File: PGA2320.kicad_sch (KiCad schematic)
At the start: 20 parts, among them J1 XH2.54-3P, J2 XH2.54-3P, J3 2P-2.54, J4 3P-2.54, P1 SDO_TO_OTHER_PGA2311, P2 CONTROLLER, U1 PGA2320

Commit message: add libs
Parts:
- U1: symbol Amplifier_Audio:PGA2320 -> PGA2320_components:PGA2320
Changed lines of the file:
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@@
     )
   )
-  (symbol (lib_id "Amplifier_Audio:PGA2320") (at 140.97 39.37 0) (unit 1)
+  (symbol (lib_id "PGA2320_components:PGA2320") (at 140.97 39.37 0) (unit 1)
     (in_bom yes) (on_board yes) (dnp no)
     (property "Reference" "U1" (at 157.48 52.07 0)

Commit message: pcb layout
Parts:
- P1: footprint Connector_Pin:Pin_D0.7mm_L6.5mm_W1.8mm_FlatFork -> Connector_Pin:Pin_D0.9mm_L10.0mm_W2.4mm_FlatFork
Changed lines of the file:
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@@
       (effects (font (size 1.27 1.27)))
     )
-    (property "Footprint" "Connector_Pin:Pin_D0.7mm_L6.5mm_W1.8mm_FlatFork" (at 180.34 125.73 0)
+    (property "Footprint" "Connector_Pin:Pin_D0.9mm_L10.0mm_W2.4mm_FlatFork" (at 180.34 125.73 0)
       (effects (font (size 1.27 1.27)) hide)
     )

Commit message: layout
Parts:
- D1, D2, D3: footprint Audio_Module:Led_1206 -> LED_SMD:LED_0805_2012Metric_Pad1.15x1.40mm_HandSolder
- R1, R2, R3: footprint Audio_Module:r_1210 -> Resistor_SMD:R_0805_2012Metric_Pad1.20x1.40mm_HandSolder
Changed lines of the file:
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@@
       (effects (font (size 1.27 1.27)))
     )
-    (property "Footprint" "Audio_Module:Led_1206" (at 54.61 77.47 0)
+    (property "Footprint" "LED_SMD:LED_0805_2012Metric_Pad1.15x1.40mm_HandSolder" (at 54.61 77.47 0)
       (effects (font (size 1.27 1.27)) hide)
     )
@@
       (effects (font (size 1.27 1.27)))
     )
-    (property "Footprint" "Audio_Module:r_1210" (at 46.99 55.372 90)
+    (property "Footprint" "Resistor_SMD:R_0805_2012Metric_Pad1.20x1.40mm_HandSolder" (at 46.99 55.372 90)
       (effects (font (size 1.27 1.27)) hide)
     )
@@
       (effects (font (size 1.27 1.27)))
     )
-    (property "Footprint" "Audio_Module:Led_1206" (at 54.61 57.15 0)
+    (property "Footprint" "LED_SMD:LED_0805_2012Metric_Pad1.15x1.40mm_HandSolder" (at 54.61 57.15 0)
       (effects (font (size 1.27 1.27)) hide)
     )
@@
       (effects (font (size 1.27 1.27)))
     )
-    (property "Footprint" "Audio_Module:r_1210" (at 46.99 67.818 90)
+    (property "Footprint" "Resistor_SMD:R_0805_2012Metric_Pad1.20x1.40mm_HandSolder" (at 46.99 67.818 90)
       (effects (font (size 1.27 1.27)) hide)
     )
@@
       (effects (font (size 1.27 1.27)))
     )
-    (property "Footprint" "Audio_Module:r_1210" (at 46.99 79.248 90)
+    (property "Footprint" "Resistor_SMD:R_0805_2012Metric_Pad1.20x1.40mm_HandSolder" (at 46.99 79.248 90)
       (effects (font (size 1.27 1.27)) hide)
     )
@@
       (effects (font (size 1.27 1.27)))
     )
-    (property "Footprint" "Audio_Module:Led_1206" (at 54.61 66.04 0)
-      (effects (font (size 1.27 1.27)) hide)
-    )
+    (property "Footprint" "LED_SMD:LED_0805_2012Metric_Pad1.15x1.40mm_HandSolder" (at 54.61 66.04 0)
+      (effects (font (size 1.27 1.27)) hide)
+    )

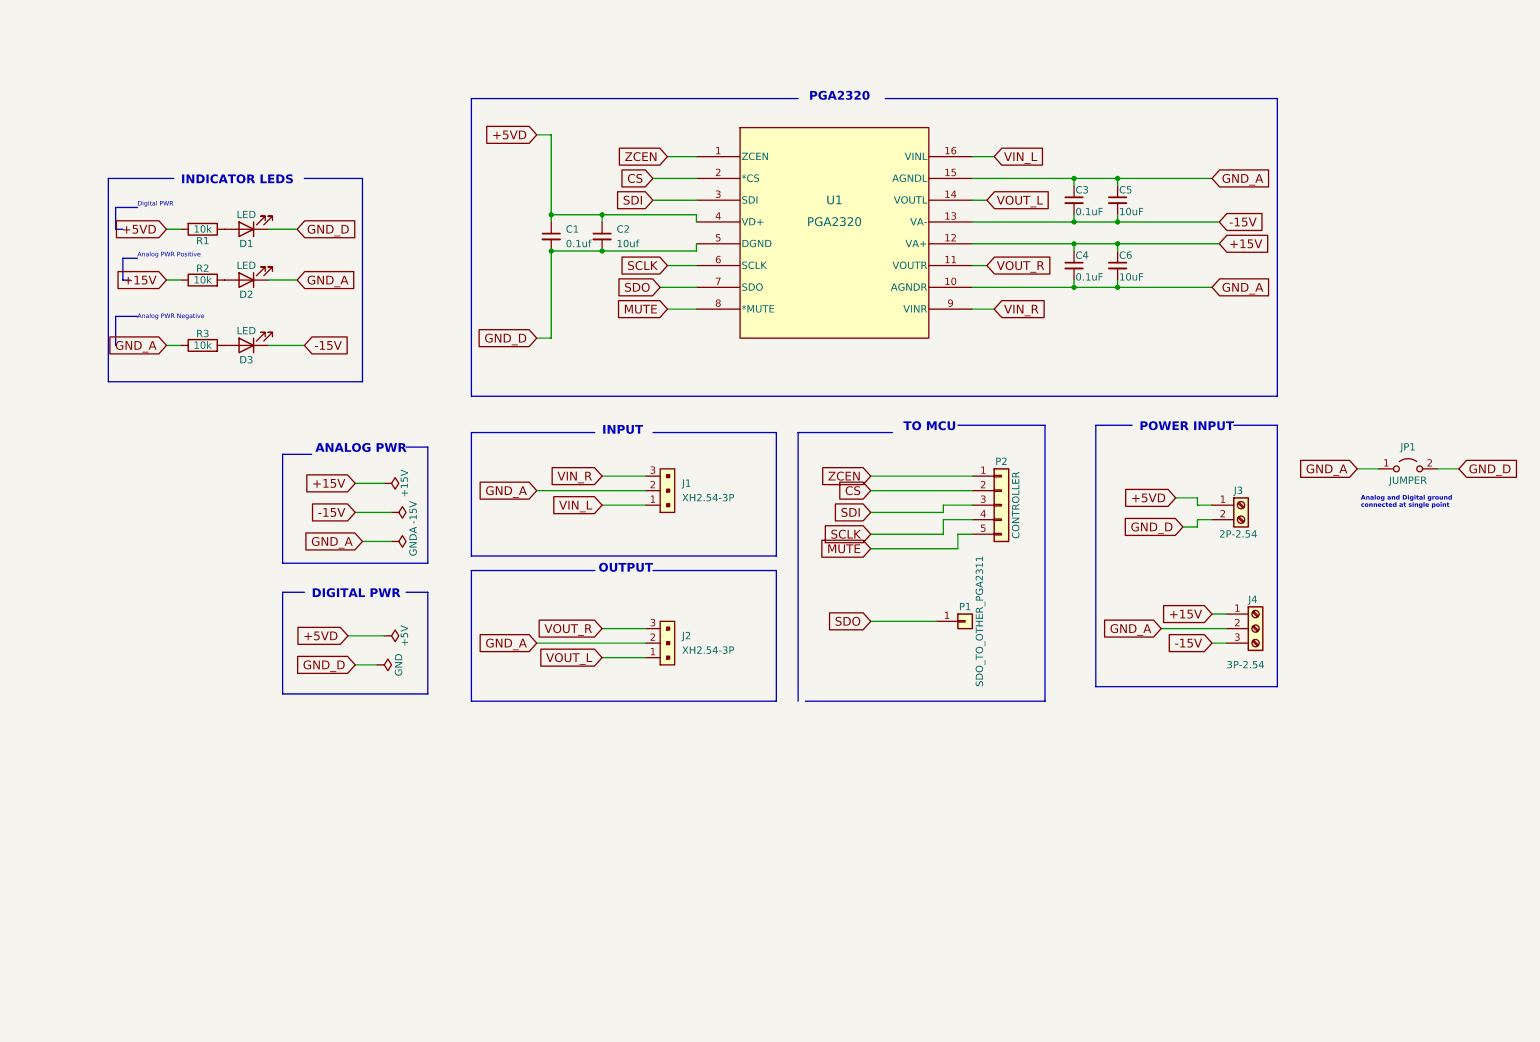
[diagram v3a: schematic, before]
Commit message: add regulator circuit
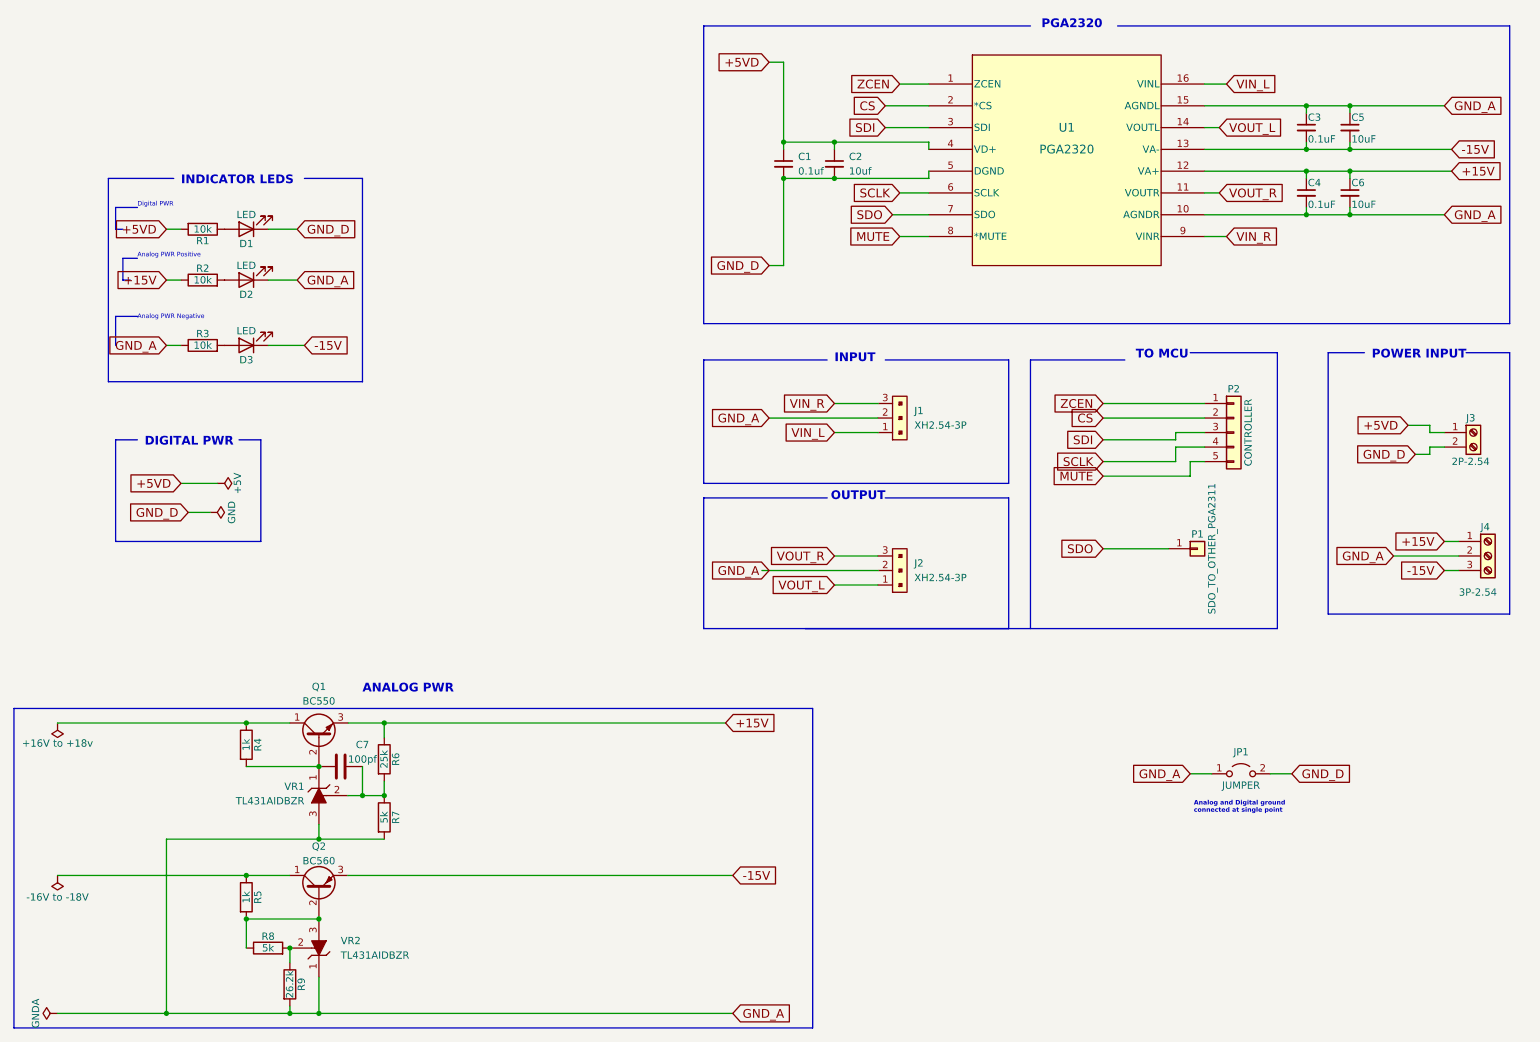
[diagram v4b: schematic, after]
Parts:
- added C7: 100pf, Capacitor_SMD:C_0805_2012Metric, symbol Device:C
- added Q1: BC550, Package_TO_SOT_THT:TO-92_Inline, symbol Transistor_BJT:BC550
- added Q2: BC560, Package_TO_SOT_THT:TO-92_Inline, symbol Transistor_BJT:BC560
- added R4, R5: 1k, Resistor_SMD:R_0805_2012Metric_Pad1.20x1.40mm_HandSolder, symbol Device:R
- added R6: 25k, Resistor_SMD:R_0805_2012Metric_Pad1.20x1.40mm_HandSolder, symbol Device:R
- added R7, R8: 5k, Resistor_SMD:R_0805_2012Metric_Pad1.20x1.40mm_HandSolder, symbol Device:R
- added R9: 26.2k, Resistor_SMD:R_0805_2012Metric_Pad1.20x1.40mm_HandSolder, symbol Device:R
- added VR1, VR2: TL431AIDBZR, digikey-footprints:SOT-23-3, symbol dk_PMIC-Voltage-Reference:TL431AIDBZR
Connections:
- net +15V: now also Q1.3 (E), R6.1
- net -15V: now also Q2.3 (E)
- net GND_A: now also R7.2, R9.2, VR1.3 (A), VR2.1 (K)
- new net: Q1.1 (C), R4.1
- new net: C7.1, Q1.2 (B), R4.2, VR1.1 (K)
- new net: R8.2, R9.1, VR2.2 (REF)
- new net: Q2.2 (B), R5.2, R8.1, VR2.3 (A)
- new net: C7.2, R6.2, R7.1, VR1.2 (REF)
- new net: Q2.1 (C), R5.1
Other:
- moved on the sheet: C1, C2, C3, C4, C5, C6, J1, J2, J3, J4, JP1, P1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

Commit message: improvements
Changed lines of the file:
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@@
     )
   )
-  (global_label "-15V" (shape input) (at 139.7 170.18 0) (fields_autoplaced)
+  (global_label "-15V" (shape output) (at 139.7 170.18 0) (fields_autoplaced)
     (effects (font (size 1.524 1.524)) (justify left))
     (property "Intersheetrefs" "${INTERSHEET_REFS}" (at 149.3777 170.18 0)
@@
     )
   )
-  (global_label "GND_A" (shape input) (at 139.7 194.31 0) (fields_autoplaced)
+  (global_label "GND_A" (shape output) (at 139.7 194.31 0) (fields_autoplaced)
     (effects (font (size 1.524 1.524)) (justify left))
     (property "Intersheetrefs" "${INTERSHEET_REFS}" (at 150.3937 194.31 0)
@@
     )
   )
-  (global_label "+15V" (shape input) (at 138.43 143.51 0) (fields_autoplaced)
+  (global_label "+15V" (shape output) (at 138.43 143.51 0) (fields_autoplaced)
     (effects (font (size 1.524 1.524)) (justify left))
     (property "Intersheetrefs" "${INTERSHEET_REFS}" (at 148.1077 143.51 0)

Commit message: improvements
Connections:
- net +16v to +18v: now reaches Q1.1 (C), R4.1
- net -16v to -18v: now reaches Q2.1 (C), R5.1
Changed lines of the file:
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@@
     (stroke (width 0) (type default))
   )
-  (polyline (pts (xy 57.15 111.76) (xy 31.75 111.76))
-    (stroke (width 0) (type default))
-  )
-  (polyline (pts (xy 31.75 111.76) (xy 31.75 93.98))
+  (polyline (pts (xy 57.15 129.54) (xy 31.75 129.54))
+    (stroke (width 0) (type default))
+  )
+  (polyline (pts (xy 31.75 129.54) (xy 31.75 93.98))
     (stroke (width 0) (type default))
   )
@@
     (stroke (width 0) (type default))
   )
+  (wire (pts (xy 43.18 119.38) (xy 45.72 119.38))
+    (stroke (width 0) (type default))
+  )
   (polyline (pts (xy 275.59 78.74) (xy 267.97 78.74))
     (stroke (width 0) (type default))
@@
     (stroke (width 0) (type default))
   )
-  (polyline (pts (xy 57.15 93.98) (xy 57.15 111.76))
+  (polyline (pts (xy 57.15 93.98) (xy 57.15 129.54))
     (stroke (width 0) (type default))
   )
@@
     (stroke (width 0) (type default))
   )
+  (wire (pts (xy 43.18 114.3) (xy 45.72 114.3))
+    (stroke (width 0) (type default))
+  )
   (wire (pts (xy 222.25 50.8) (xy 224.79 50.8))
     (stroke (width 0) (type default))
@@
   )
   (polyline (pts (xy 35.56 62.23) (xy 33.02 62.23))
+    (stroke (width 0) (type default))
+  )
+  (wire (pts (xy 43.18 125.73) (xy 45.72 125.73))
     (stroke (width 0) (type default))
   )
@@
     (effects (font (size 1.524 1.524) (thickness 0.3048) bold) (justify left bottom))
   )
+  (label "-16v to -18v" (at 21.59 170.18 0) (fields_autoplaced)
+    (effects (font (size 1.27 1.27)) (justify left bottom))
+  )
+  (label "GND_A" (at 21.59 194.31 0) (fields_autoplaced)
+    (effects (font (size 1.27 1.27)) (justify left bottom))
+  )
+  (label "+16v to +18v" (at 21.59 143.51 0) (fields_autoplaced)
+    (effects (font (size 1.27 1.27)) (justify left bottom))
+  )
+  (global_label "-15V" (shape output) (at 43.18 119.38 180) (fields_autoplaced)
+    (effects (font (size 1.524 1.524)) (justify right))
+    (property "Intersheetrefs" "${INTERSHEET_REFS}" (at 33.5023 119.38 0)
+      (effects (font (size 1.524 1.524)) (justify right) hide)
+    )
+  )
   (global_label "GND_A" (shape input) (at 63.5 66.04 0) (fields_autoplaced)
     (effects (font (size 1.524 1.524)) (justify left))
@@
     (property "Intersheetrefs" "${INTERSHEET_REFS}" (at 160.2428 58.3248 0)
       (effects (font (size 1.27 1.27)) (justify right) hide)
+    )
+  )
+  (global_label "GND_A" (shape output) (at 43.18 125.73 180) (fields_autoplaced)
+    (effects (font (size 1.524 1.524)) (justify right))
+    (property "Intersheetrefs" "${INTERSHEET_REFS}" (at 32.4863 125.73 0)
+      (effects (font (size 1.524 1.524)) (justify right) hide)
     )
   )
@@
     )
   )
+  (global_label "+15V" (shape output) (at 43.18 114.3 180) (fields_autoplaced)
+    (effects (font (size 1.524 1.524)) (justify right))
+    (property "Intersheetrefs" "${INTERSHEET_REFS}" (at 33.5023 114.3 0)
+      (effects (font (size 1.524 1.524)) (justify right) hide)
+    )
+  )
   (global_label "SCLK" (shape input) (at 168.91 50.8 180) (fields_autoplaced)
     (effects (font (size 1.524 1.524)) (justify right))
@@
         (path "/5b7801f4-55a7-4c74-b3bf-bacecbb4cf6a"
           (reference "C6") (unit 1)
-        )
-      )
-    )
-  )
-  (symbol (lib_id "power:PWR_FLAG") (at 21.59 194.31 90) (unit 1)
-    (in_bom yes) (on_board yes) (dnp no)
-    (property "Reference" "#PWR05" (at 27.94 194.31 0)
-      (effects (font (size 1.27 1.27)) hide)
-    )
-    (property "Value" "GNDA" (at 17.78 194.31 0)
-      (effects (font (size 1.27 1.27)))
-    )
-    (property "Footprint" "" (at 21.59 194.31 0)
-      (effects (font (size 1.27 1.27)) hide)
-    )
-    (property "Datasheet" "~" (at 21.59 194.31 0)
-      (effects (font (size 1.27 1.27)) hide)
-    )
-    (pin "1")
-    (instances
-      (project "PGA2320"
-        (path "/3c367401-208f-4628-9cce-4b3b1ae65d20"
-          (reference "#PWR05") (unit 1)
-        )
-      )
-      (project "pga2311"
-        (path "/5b7801f4-55a7-4c74-b3bf-bacecbb4cf6a"
-          (reference "#PWR05") (unit 1)
         )
       )
@@
     )
   )
-  (symbol (lib_name "PWR_FLAG_2") (lib_id "power:PWR_FLAG") (at 21.59 170.18 180) (unit 1)
-    (in_bom yes) (on_board yes) (dnp no)
-    (property "Reference" "#PWR04" (at 21.59 172.72 0)
-      (effects (font (size 1.27 1.27)) hide)
-    )
-    (property "Value" "-16V to -18V" (at 21.59 173.99 0)
-      (effects (font (size 1.27 1.27)))
-    )
-    (property "Footprint" "" (at 21.59 170.18 0)
-      (effects (font (size 1.27 1.27)) hide)
-    )
-    (property "Datasheet" "~" (at 21.59 170.18 0)
-      (effects (font (size 1.27 1.27)) hide)
-    )
-    (pin "1")
-    (instances
-      (project "PGA2320"
-        (path "/3c367401-208f-4628-9cce-4b3b1ae65d20"
-          (reference "#PWR04") (unit 1)
-        )
-      )
-      (project "pga2311"
-        (path "/5b7801f4-55a7-4c74-b3bf-bacecbb4cf6a"
-          (reference "#PWR04") (unit 1)
-        )
-      )
-    )
-  )
   (symbol (lib_id "Transistor_BJT:BC550") (at 67.31 146.05 90) (unit 1)
     (in_bom yes) (on_board yes) (dnp no) (fields_autoplaced)
@@
         (path "/5b7801f4-55a7-4c74-b3bf-bacecbb4cf6a"
           (reference "J3") (unit 1)
+        )
+      )
+    )
+  )
+  (symbol (lib_id "power:PWR_FLAG") (at 45.72 125.73 270) (unit 1)
+    (in_bom yes) (on_board yes) (dnp no) (fields_autoplaced)
+    (property "Reference" "#FLG03" (at 47.625 125.73 0)
+      (effects (font (size 1.27 1.27)) hide)
+    )
+    (property "Value" "PWR_FLAG" (at 49.53 125.73 90)
+      (effects (font (size 1.27 1.27)) (justify left))
+    )
+    (property "Footprint" "" (at 45.72 125.73 0)
+      (effects (font (size 1.27 1.27)) hide)
+    )
+    (property "Datasheet" "~" (at 45.72 125.73 0)
+      (effects (font (size 1.27 1.27)) hide)
+    )
+    (pin "1")
+    (instances
+      (project "PGA2320"
+        (path "/3c367401-208f-4628-9cce-4b3b1ae65d20"
+          (reference "#FLG03") (unit 1)
         )
       )
@@
     )
   )
-  (symbol (lib_name "PWR_FLAG_1") (lib_id "power:PWR_FLAG") (at 21.59 143.51 180) (unit 1)
-    (in_bom yes) (on_board yes) (dnp no)
-    (property "Reference" "#PWR02" (at 21.59 139.7 0)
-      (effects (font (size 1.27 1.27)) hide)
-    )
-    (property "Value" "+16V to +18v" (at 21.59 147.066 0)
-      (effects (font (size 1.27 1.27)))
-    )
-    (property "Footprint" "" (at 21.59 143.51 0)
-      (effects (font (size 1.27 1.27)) hide)
-    )
-    (property "Datasheet" "~" (at 21.59 143.51 0)
-      (effects (font (size 1.27 1.27)) hide)
-    )
-    (pin "1")
-    (instances
-      (project "PGA2320"
-        (path "/3c367401-208f-4628-9cce-4b3b1ae65d20"
-          (reference "#PWR02") (unit 1)
-        )
-      )
-      (project "pga2311"
-        (path "/5b7801f4-55a7-4c74-b3bf-bacecbb4cf6a"
-          (reference "#PWR06") (unit 1)
+  (symbol (lib_id "power:PWR_FLAG") (at 45.72 114.3 270) (unit 1)
+    (in_bom yes) (on_board yes) (dnp no) (fields_autoplaced)
+    (property "Reference" "#FLG01" (at 47.625 114.3 0)
+      (effects (font (size 1.27 1.27)) hide)
+    )
+    (property "Value" "PWR_FLAG" (at 49.53 114.3 90)
+      (effects (font (size 1.27 1.27)) (justify left))
+    )
+    (property "Footprint" "" (at 45.72 114.3 0)
+      (effects (font (size 1.27 1.27)) hide)
+    )
+    (property "Datasheet" "~" (at 45.72 114.3 0)
+      (effects (font (size 1.27 1.27)) hide)
+    )
+    (pin "1")
+    (instances
+      (project "PGA2320"
+        (path "/3c367401-208f-4628-9cce-4b3b1ae65d20"
+          (reference "#FLG01") (unit 1)
         )
       )
@@
         )
       )
+    )
+  )
+  (symbol (lib_id "power:PWR_FLAG") (at 45.72 119.38 270) (unit 1)
+    (in_bom yes) (on_board yes) (dnp no) (fields_autoplaced)
+    (property "Reference" "#FLG02" (at 47.625 119.38 0)
+      (effects (font (size 1.27 1.27)) hide)
+    )
+    (property "Value" "PWR_FLAG" (at 49.53 119.38 90)
+      (effects (font (size 1.27 1.27)) (justify left))
+    )
+    (property "Footprint" "" (at 45.72 119.38 0)
+      (effects (font (size 1.27 1.27)) hide)
+    )
+    (property "Datasheet" "~" (at 45.72 119.38 0)
+      (effects (font (size 1.27 1.27)) hide)
+    )
+    (pin "1")
+    (instances
+      (project "PGA2320"
+        (path "/3c367401-208f-4628-9cce-4b3b1ae65d20"
+          (reference "#FLG02") (unit 1)
+        )
+      )
